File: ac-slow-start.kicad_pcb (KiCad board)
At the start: 2 copper layers, 110 x 35 mm, 14 parts, among them J1 Conn_01x02_Male, J2 Conn_01x02_Male, J3 Conn_01x02_Female, J4 Conn_01x02_Female, J5 Conn_01x02_Female, J6 Conn_01x02_Female, K1 G4A-1A-PE DC24

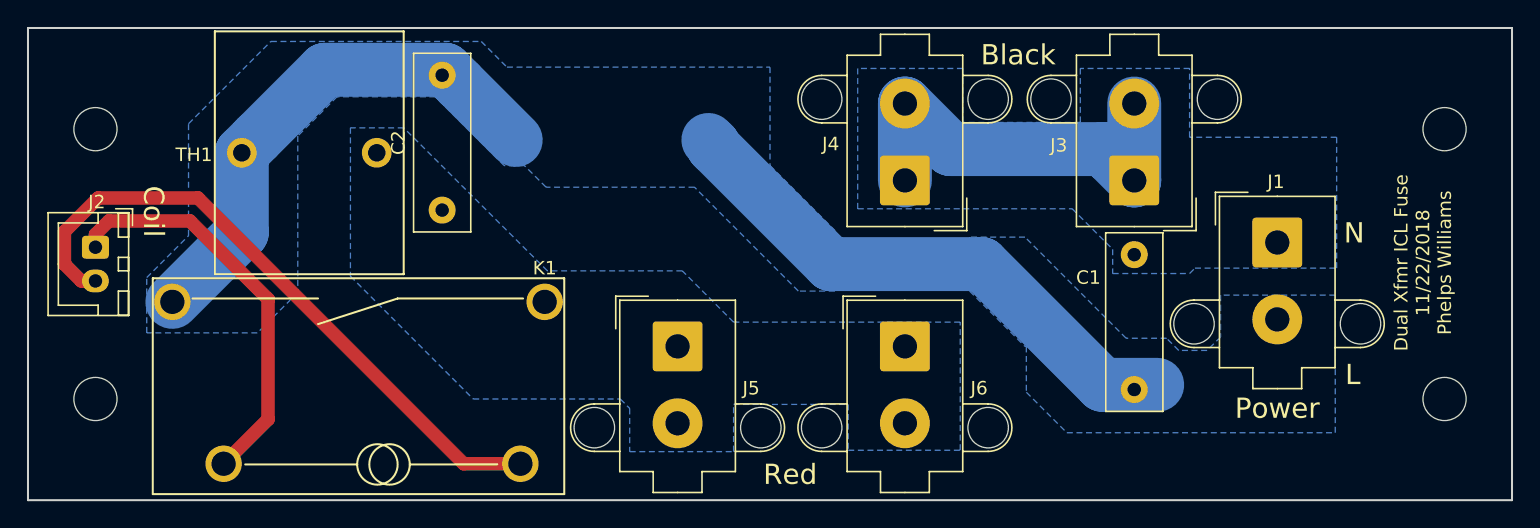
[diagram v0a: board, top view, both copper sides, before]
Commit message: Updating with new smaller footprint
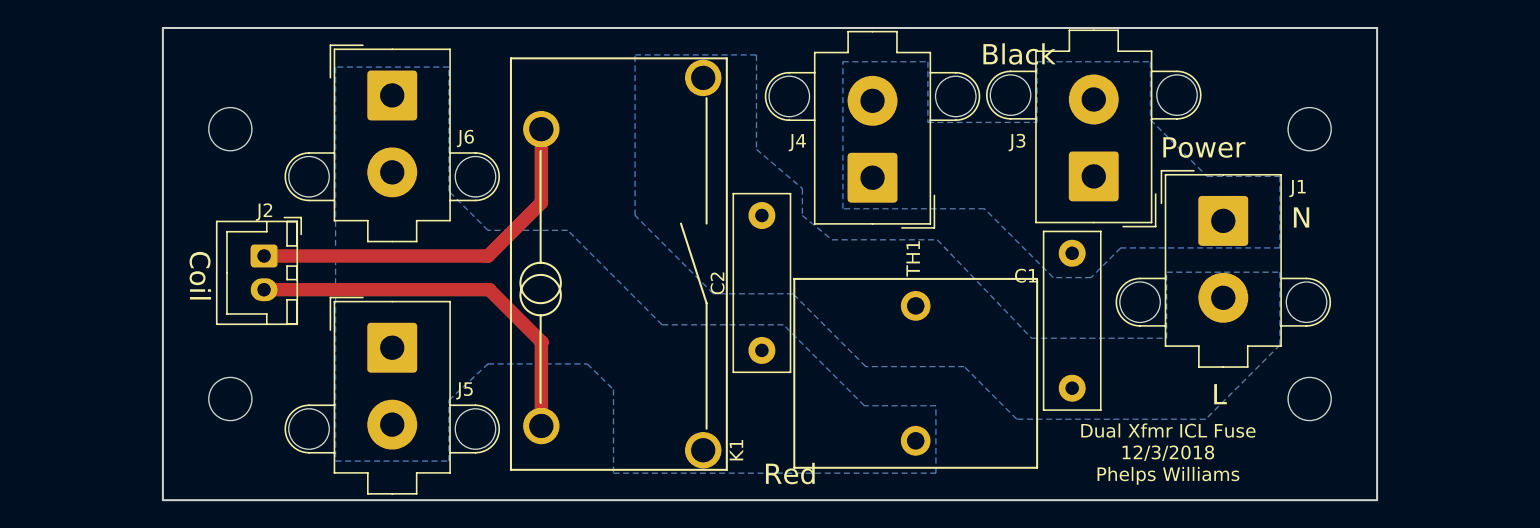
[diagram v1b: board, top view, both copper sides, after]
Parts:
- moved TH1 47.8 mm to (95.8, 75.6), turned to 180 degrees
- moved J6 42.3 mm to (57.0, 55.0)
- moved C2 25.9 mm to (84.4, 73.9)
- moved K1 21.3 mm to (73.8, 67.5), turned to 270 degrees
- moved J5 21.2 mm to (57.0, 73.7)
- moved J2 12.5 mm to (47.5, 66.9)
- moved H1 10.0 mm to (45.0, 77.5)
- moved H2 10.0 mm to (125.0, 77.5)
- moved H3 10.0 mm to (45.0, 57.5)
- moved H4 10.0 mm to (125.0, 57.5)
- moved C1 4.60 mm to (107.4, 66.7)
- moved J1 4.31 mm to (118.6, 64.3)
- moved J3 3.01 mm to (109.0, 61.0)
- moved J4 2.41 mm to (92.6, 61.1)
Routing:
- net Net-(C1-Pad2): track 79.0 -> 0.00 mm
- net Net-(C1-Pad1): track 30.8 -> 0.00 mm
- net Net-(J2-Pad2): track 48.2 -> 28.4 mm
- net Net-(J2-Pad1): track 30.1 -> 27.6 mm
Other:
- board size 110 x 35 mm -> 90 x 35 mm
- board text added: "Dual Xfmr ICL Fuse 12/3/2018 Phelps Williams"
- board text removed: "Dual Xfmr ICL Fuse 11/22/2018 Phelps Williams"

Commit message: ac slow start tweaks from mfg
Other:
- outline, holes or cut-outs redrawn
- board text added: "AC IN"
- board text added: "Dual Xfmr ICL 12/3/2018 Phelps Williams"
- board text removed: "Dual Xfmr ICL Fuse 12/3/2018 Phelps Williams"
- board text removed: "Power"
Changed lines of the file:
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@@
     (0 F.Cu signal)
     (31 B.Cu signal)
-    (32 B.Adhes user)
-    (33 F.Adhes user)
-    (34 B.Paste user)
-    (35 F.Paste user)
+    (32 B.Adhes user hide)
+    (33 F.Adhes user hide)
+    (34 B.Paste user hide)
+    (35 F.Paste user hide)
     (36 B.SilkS user)
     (37 F.SilkS user)
@@
     (40 Dwgs.User user)
     (41 Cmts.User user)
-    (42 Eco1.User user)
-    (43 Eco2.User user)
+    (42 Eco1.User user hide)
+    (43 Eco2.User user hide)
     (44 Edge.Cuts user)
     (45 Margin user)
@@
   )
   (setup
-    (last_trace_width 1)
+    (last_trace_width 0.25)
     (user_trace_width 1)
     (user_trace_width 2)
@@
     (visible_elements FFFDFF7F)
     (pcbplotparams
-      (layerselection 0x010fc_ffffffff)
+      (layerselection 0x010f0_ffffffff)
       (usegerberextensions false)
-      (usegerberattributes false)
+      (usegerberattributes true)
       (usegerberadvancedattributes false)
       (creategerberjobfile false)
@@
       (psa4output false)
       (plotreference true)
-      (plotvalue true)
+      (plotvalue false)
       (plotinvisibletext false)
       (padsonsilk false)
@@
       (outputformat 1)
       (mirror false)
-      (drillshape 1)
+      (drillshape 0)
       (scaleselection 1)
-      (outputdirectory ""))
+      (outputdirectory "gerber/"))
   )
   (net 0 "")
@@
     (descr "C, Rect series, Radial, pin pitch=10.00mm, , length*width=13*4mm^2, Capacitor, http://www.wima.com/EN/WIMA_FKS_3.pdf, http://www.wima.com/EN/WIMA_MKS_4.pdf")
     (tags "C Rect series Radial pin pitch 10.00mm  length 13mm width 4mm Capacitor")
-    (fp_text reference C1 (at 1.7 3.4) (layer F.SilkS)
+    (fp_text reference C1 (at -0.98 3.13) (layer F.SilkS)
       (effects (font (size 1 1) (thickness 0.15)))
     )
@@
   (module p_ptc:B59215J0130A020 (layer F.Cu)
     (at 95.8 75.6 180)
-    (fp_text reference TH1 (at 0.15 8.55 -90) (layer F.SilkS)
+    (fp_text reference TH1 (at 7.37 7.79) (layer F.SilkS)
       (effects (font (size 1 1) (thickness 0.15)))
     )
@@
     (descr "C, Rect series, Radial, pin pitch=10.00mm, , length*width=13*4mm^2, Capacitor, http://www.wima.com/EN/WIMA_FKS_3.pdf, http://www.wima.com/EN/WIMA_MKS_4.pdf")
     (tags "C Rect series Radial pin pitch 10.00mm  length 13mm width 4mm Capacitor")
-    (fp_text reference C2 (at 5 -3.25 90) (layer F.SilkS)
+    (fp_text reference C2 (at 12.42 -1.17 180) (layer F.SilkS)
       (effects (font (size 1 1) (thickness 0.15)))
     )
@@
     )
   )
-  (gr_line (start 92.3 76.7) (end 98.8 76.7) (layer Eco2.User) (width 1.6))
-  (gr_line (start 86.4 70.8) (end 78.4 70.8) (layer Eco2.User) (width 1.6))
-  (gr_line (start 92.3 76.7) (end 86.4 70.8) (layer Eco2.User) (width 1.6))
-  (gr_line (start 90.7 64.6) (end 99.3 64.6) (layer Eco2.User) (width 1.6))
-  (gr_line (start 89 62.9) (end 90.7 64.6) (layer Eco2.User) (width 1.6))
-  (gr_line (start 89 60) (end 89 62.9) (layer Eco2.User) (width 1.6))
-  (gr_line (start 112.5 67.2) (end 123.7 67.2) (layer Eco2.User) (width 1.6))
+  (gr_line (start 92.3 76.7) (end 98.8 76.7) (layer Edge.Cuts) (width 1.6))
+  (gr_line (start 86.4 70.8) (end 78.4 70.8) (layer Edge.Cuts) (width 1.6))
+  (gr_line (start 92.3 76.7) (end 86.4 70.8) (layer Edge.Cuts) (width 1.6))
+  (gr_line (start 90.7 64.6) (end 99.3 64.6) (layer Edge.Cuts) (width 1.6))
+  (gr_line (start 89 62.9) (end 90.7 64.6) (layer Edge.Cuts) (width 1.6))
+  (gr_line (start 89 60) (end 89 62.9) (layer Edge.Cuts) (width 1.6))
+  (gr_line (start 112.5 67.2) (end 123.7 67.2) (layer Edge.Cuts) (width 1.6))
   (gr_text Coil (at 42.7 68.4 270) (layer F.SilkS)
     (effects (font (size 1.5 1.5) (thickness 0.3)))
@@
     (effects (font (size 1.5 1.5) (thickness 0.3)))
   )
-  (gr_text Power (at 117.1 58.9) (layer F.SilkS)
+  (gr_text "AC IN" (at 117.33 59.52) (layer F.SilkS)
     (effects (font (size 1.5 1.5) (thickness 0.3)))
   )
-  (gr_text Red (at 86.5 83.1) (layer F.SilkS)
+  (gr_text Red (at 57.19 67.97) (layer F.SilkS)
     (effects (font (size 1.5 1.5) (thickness 0.3)))
   )
-  (gr_text Black (at 103.4 52) (layer F.SilkS)
+  (gr_text Black (at 100.86 60.64) (layer F.SilkS)
     (effects (font (size 1.5 1.5) (thickness 0.3)))
   )
-  (gr_text "Dual Xfmr ICL Fuse\n12/3/2018\nPhelps Williams" (at 114.5 81.5) (layer F.SilkS)
+  (gr_text "Dual Xfmr ICL\n12/3/2018\nPhelps Williams" (at 114.5 81.5) (layer F.SilkS)
     (effects (font (size 1 1) (thickness 0.2)))
   )
